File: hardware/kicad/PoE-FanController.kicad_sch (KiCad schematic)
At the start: 26 parts, among them J2 FAN1, J3 FAN2, J4 FAN3, J5 FAN4, J8 Waveshare_ESP32P4POEETH, U1 LM2587-12

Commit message: hw+fw: add orange prog/OTA LED (issue #89)
Hardware:
- R13 (330Ω THT, P7.62mm) placed at PCB (25, 64)
- LED2 (orange 3mm THT, Wurth 150060AS75000) placed at PCB (31, 58)
  next to LED1 (green status LED)
- Circuit: PROG_LED → R13 → PROG_LED_A → LED2 anode → GND
- J8 pin 22 (GPIO15) wired to PROG_LED net (was NC)
- ERC: 0 errors · DRC: 0 real errors · 0 courtyard overlaps
- BOM updated with R13 and LED2 entries

Firmware:
- pins.h: add PROG_LED_PIN (GPIO15)
- ota.cpp: add ota_init() to configure GPIO15; LED2 flickers on each
  OTA chunk write, holds HIGH on success, LOW on error
- main.cpp: call ota_init() in setup()

Co-authored-by: Copilot <223556219+Copilot@users.noreply.github.com>
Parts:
- added LED2: LED_ORANGE, LED_THT:LED_D3.0mm, symbol Custom:LED
- added R4: 10k, Resistor_THT:R_Axial_DIN0207_L6.3mm_D2.5mm_P7.62mm_Horizontal, symbol Custom:R
- R13: renamed from R4; value 10k -> 330R
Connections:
- net NTC_ADC: now also R4.2; no longer R13.2
- net PROG_LED: now reaches R13.1
- net PROG_LED: now also J8.22 (NC)
- new net PROG_LED_A: LED2.1 (A), R13.2
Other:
- note added: "Prog LED (OTA)"
- moved on the sheet: R13

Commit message: hw(oq): resolve OQ-02 — fix +5V pins on J8 (39/40 not 2/4)
Confirmed from Waveshare ESP32-P4-ETH schematic (Interface section):
  - Pin 39 = VSYS: +5V PoE PD main output
  - Pin 40 = VBUS: +5V USB source
  - Pins 2 and 4 are NOT power pins (previously wrong assumption)

Changes in components.py:
  - J8 pin 39: NC -> +5V power_out (VSYS)
  - J8 pin 40: NC -> +5V power_out (VBUS)
  - J8 pin 2:  +5V power_out -> NC
  - J8 pin 4:  +5V power_out -> NC
  - Clear OQ-02 PENDING marker
  - Update placement net connections accordingly

Schematic regenerated; ERC: 0 errors; DRC: 0 errors.

Closes #85

Co-authored-by: Copilot <223556219+Copilot@users.noreply.github.com>
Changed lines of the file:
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@@
     (instances (project "PoE-FanController" (path "/" (reference "#PWR039") (unit 1))))
   )
-  (symbol (lib_id "power:+5V") (at 106.6800 128.2700 0)
+  (symbol (lib_id "power:+5V") (at 76.2000 176.5300 0)
     (unit 1) (exclude_from_sim no) (in_bom yes) (on_board yes) (dnp no)
     (fields_autoplaced yes)
     (property "Reference" "#PWR040"
-      (at 106.6800 130.8100 0)
+      (at 76.2000 179.0700 0)
       (hide yes)
       (effects (font (size 1.27 1.27))))
     (property "Value" "+5V"
-      (at 106.6800 125.7300 0)
+      (at 76.2000 173.9900 0)
       (effects (font (size 1.27 1.27))))
     (property "Footprint" ""
-      (at 106.6800 128.2700 0)
+      (at 76.2000 176.5300 0)
       (hide yes)
       (effects (font (size 1.27 1.27))))
     (property "Datasheet" ""
-      (at 106.6800 128.2700 0)
+      (at 76.2000 176.5300 0)
       (hide yes)
       (effects (font (size 1.27 1.27))))
@@
     (instances (project "PoE-FanController" (path "/" (reference "#PWR040") (unit 1))))
   )
-  (symbol (lib_id "power:+5V") (at 106.6800 130.8100 0)
+  (symbol (lib_id "power:GND") (at 106.6800 133.3500 0)
     (unit 1) (exclude_from_sim no) (in_bom yes) (on_board yes) (dnp no)
     (fields_autoplaced yes)
     (property "Reference" "#PWR041"
-      (at 106.6800 133.3500 0)
-      (hide yes)
-      (effects (font (size 1.27 1.27))))
-    (property "Value" "+5V"
-      (at 106.6800 128.2700 0)
-      (effects (font (size 1.27 1.27))))
-    (property "Footprint" ""
-      (at 106.6800 130.8100 0)
-      (hide yes)
-      (effects (font (size 1.27 1.27))))
-    (property "Datasheet" ""
-      (at 106.6800 130.8100 0)
-      (hide yes)
-      (effects (font (size 1.27 1.27))))
-    (pin "1")
-    (instances (project "PoE-FanController" (path "/" (reference "#PWR041") (unit 1))))
-  )
-  (symbol (lib_id "power:GND") (at 106.6800 133.3500 0)
-    (unit 1) (exclude_from_sim no) (in_bom yes) (on_board yes) (dnp no)
-    (fields_autoplaced yes)
-    (property "Reference" "#PWR042"
       (at 106.6800 135.8900 0)
       (hide yes)
@@
       (effects (font (size 1.27 1.27))))
     (pin "1")
-    (instances (project "PoE-FanController" (path "/" (reference "#PWR042") (unit 1))))
+    (instances (project "PoE-FanController" (path "/" (reference "#PWR041") (unit 1))))
   )
   (global_label "FAN2_PWM"
@@
     (unit 1) (exclude_from_sim no) (in_bom yes) (on_board yes) (dnp no)
     (fields_autoplaced yes)
-    (property "Reference" "#PWR043"
+    (property "Reference" "#PWR042"
       (at 106.6800 146.0500 0)
       (hide yes)
@@
       (effects (font (size 1.27 1.27))))
     (pin "1")
-    (instances (project "PoE-FanController" (path "/" (reference "#PWR043") (unit 1))))
+    (instances (project "PoE-FanController" (path "/" (reference "#PWR042") (unit 1))))
   )
   (global_label "FAN4_TACH"
@@
     (unit 1) (exclude_from_sim no) (in_bom yes) (on_board yes) (dnp no)
     (fields_autoplaced yes)
-    (property "Reference" "#PWR044"
+    (property "Reference" "#PWR043"
       (at 106.6800 153.6700 0)
       (hide yes)
@@
       (effects (font (size 1.27 1.27))))
     (pin "1")
-    (instances (project "PoE-FanController" (path "/" (reference "#PWR044") (unit 1))))
+    (instances (project "PoE-FanController" (path "/" (reference "#PWR043") (unit 1))))
   )
   (global_label "PROG_LED"
@@
     (unit 1) (exclude_from_sim no) (in_bom yes) (on_board yes) (dnp no)
     (fields_autoplaced yes)
-    (property "Reference" "#PWR045"
+    (property "Reference" "#PWR044"
       (at 106.6800 176.5300 0)
       (hide yes)
@@
       (hide yes)
       (effects (font (size 1.27 1.27))))
+    (pin "1")
+    (instances (project "PoE-FanController" (path "/" (reference "#PWR044") (unit 1))))
+  )
+  (symbol (lib_id "power:+5V") (at 106.6800 176.5300 0)
+    (unit 1) (exclude_from_sim no) (in_bom yes) (on_board yes) (dnp no)
+    (fields_autoplaced yes)
+    (property "Reference" "#PWR045"
+      (at 106.6800 179.0700 0)
+      (hide yes)
+      (effects (font (size 1.27 1.27))))
+    (property "Value" "+5V"
+      (at 106.6800 173.9900 0)
+      (effects (font (size 1.27 1.27))))
+    (property "Footprint" ""
+      (at 106.6800 176.5300 0)
+      (hide yes)
+      (effects (font (size 1.27 1.27))))
+    (property "Datasheet" ""
+      (at 106.6800 176.5300 0)
+      (hide yes)
+      (effects (font (size 1.27 1.27))))

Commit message: hw(schematic): add J6/R14/R15/LED6 and DS18B20_DATA/PROBE_LED nets
T001: Add Conn_1x03 (J6 Molex KK-254), R14 (4.7kΩ pull-up), R15 (330Ω),
      LED6 (green 3mm) to schematic generator with section header.
T002: Update J8 symbol/placement — pin 27 NC→DS18B20_DATA (GPIO19),
      pin 28 NC→PROBE_LED (GPIO20).
T003: Regenerated PoE-FanController.kicad_sch — J6/R14/R15/LED6 confirmed present.
T004: ERC clean — 0 errors, 83 pre-existing warnings (lib_symbol_mismatch).

Closes #101
Closes #102
Closes #103
Closes #104
Issue: #97

Co-authored-by: Copilot <223556219+Copilot@users.noreply.github.com>
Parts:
- added J6: Molex_KK254_3pin, Connector_Molex:Molex_KK-254_AE-6410-03A_1x03_P2.54mm_Vertical, symbol Custom:Conn_1x03
- added LED6: LED_GREEN, LED_THT:LED_D3.0mm, symbol Custom:LED
- added R14: 4k7, Resistor_THT:R_Axial_DIN0207_L6.3mm_D2.5mm_P7.62mm_Horizontal, symbol Custom:R
- added R15: 330R, Resistor_THT:R_Axial_DIN0207_L6.3mm_D2.5mm_P7.62mm_Horizontal, symbol Custom:R
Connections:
- net DS18B20_DATA: now reaches J8.27 (DS18B20_DATA)
- net DS18B20_DATA: now also J6.2 (DATA), R14.2
- net PROBE_LED: now reaches J8.28 (PROBE_LED)
- net PROBE_LED: now also R15.1
- new net PROBE_LED_A: LED6.1 (A), R15.2
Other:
- note added: "DS18B20 Temperature Probe (J6 / R14 / R15 / LED6)"

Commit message: hw: replace J2-J5 fan headers with keyed Molex KK-254 footprints (#100)
* docs(#100): add feature spec and technical plan for keyed fan headers

Add planning artifacts for Issue #100 - replacing unkeyed J2-J5 pin header
footprints with shrouded Molex KK-254 keyed connectors.

Key decisions documented in plan.md:
- Target footprint: Connector_Molex:Molex_KK-254_AE-6410-04A_1x04_P2.54mm_Vertical
  (22-23-2041 named in issue not present in KiCad 10.0 library; AE-6410-04A is
  the standard-library equivalent — same family, confirmed available)
- J6 already uses the 3-pin sibling (AE-6410-03A); this is established precedent
- Two generator edits required: s.define() + s.component() in components.py
- PCB: manual KiCad GUI only per P-KI-07; courtyard grows from ~2mm to 6.8mm
  perpendicular to pin row — documented with clearance assessment
- BOM §2.2 MAJOR amendment required (47053-1000 → 22-23-2041)
- No firmware changes, no isolation concerns, no power budget impact

Satisfies constitution principle P-HW-09 (amendment v3.2.0).

Files added:
  docs/features/keyed-fan-headers/spec.md
  docs/features/keyed-fan-headers/plan.md

* fix(docs): update constitution version and amend J2–J5 BOM to keyed headers

* docs: add architecture notes for keyed fan headers (J2–J5) feature

* docs(#100): add task breakdown and GitHub sub-issues for keyed fan headers (T001-T009, issues #120-#128)

* hw(#100): update J2-J5 footprint in generator and regenerate schematic

- T001: add Connector_Molex library entry to hardware/kicad/fp-lib-table
- T002: update Fan_Header define() and component() footprint to
  Connector_Molex:Molex_KK-254_AE-6410-04A_1x04_P2.54mm_Vertical
- T002: update Fan_Header datasheet URL to Molex 22-23-2041 product page
- T003: regenerate PoE-FanController.kicad_sch (4 instances updated)
- T004: ERC passes - 0 error-severity violations

Refs #120
Refs #121
Refs #122
Refs #123

Co-authored-by: Copilot <223556219+Copilot@users.noreply.github.com>

* hw(#100): swap J2-J5 PCB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
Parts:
- J2, J3, J4, J5: footprint Connector_PinHeader_2.54mm:PinHeader_1x04_P2.54mm_Vertical -> Connector_Molex:Molex_KK-254_AE-6410-04A_1x04_P2.54mm_Vertical
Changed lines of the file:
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@@
       (at 331.4700 82.5500 0)
       (effects (font (size 1.27 1.27))))
-    (property "Footprint" "Connector_PinHeader_2.54mm:PinHeader_1x04_P2.54mm_Vertical"
+    (property "Footprint" "Connector_Molex:Molex_KK-254_AE-6410-04A_1x04_P2.54mm_Vertical"
       (at 330.2000 81.2800 0)
       (hide yes)
@@
       (at 331.4700 113.0300 0)
       (effects (font (size 1.27 1.27))))
-    (property "Footprint" "Connector_PinHeader_2.54mm:PinHeader_1x04_P2.54mm_Vertical"
+    (property "Footprint" "Connector_Molex:Molex_KK-254_AE-6410-04A_1x04_P2.54mm_Vertical"
       (at 330.2000 111.7600 0)
       (hide yes)
@@
       (at 331.4700 143.5100 0)
       (effects (font (size 1.27 1.27))))
-    (property "Footprint" "Connector_PinHeader_2.54mm:PinHeader_1x04_P2.54mm_Vertical"
+    (property "Footprint" "Connector_Molex:Molex_KK-254_AE-6410-04A_1x04_P2.54mm_Vertical"
       (at 330.2000 142.2400 0)
       (hide yes)
@@
       (at 331.4700 173.9900 0)
       (effects (font (size 1.27 1.27))))
-    (property "Footprint" "Connector_PinHeader_2.54mm:PinHeader_1x04_P2.54mm_Vertical"
+    (property "Footprint" "Connector_Molex:Molex_KK-254_AE-6410-04A_1x04_P2.54mm_Vertical"
       (at 330.2000 172.7200 0)
       (hide yes)

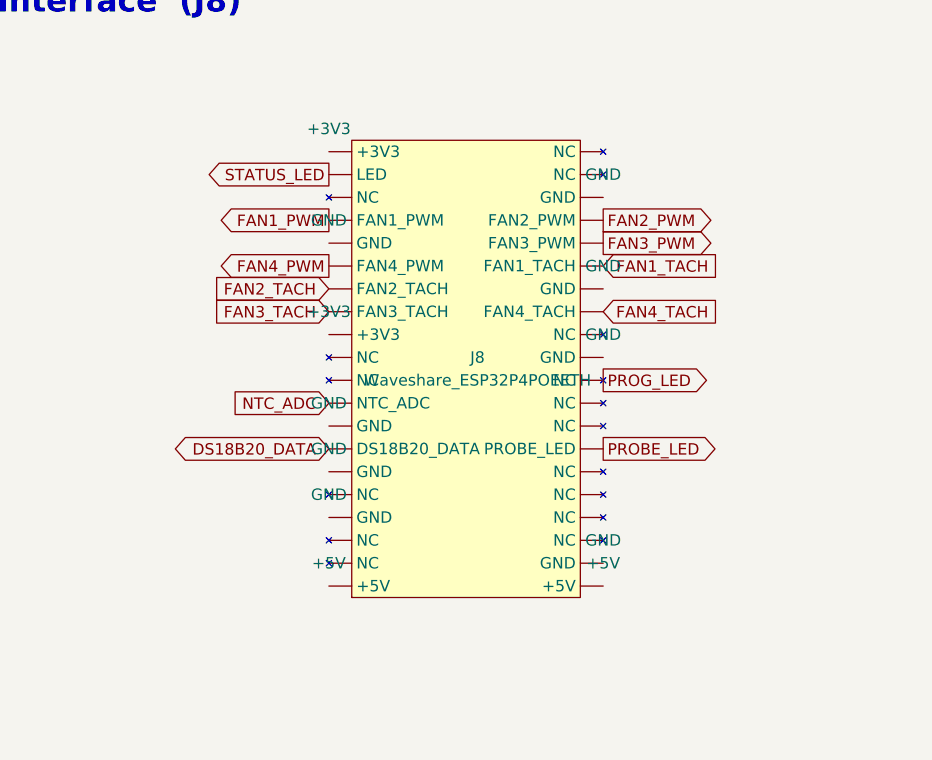
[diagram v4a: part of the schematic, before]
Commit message: fix(hw): correct J8 pin layout to consecutive columns (#133)
The Waveshare ESP32-P4-POE-ETH (SKU 32088) 2x20 header uses CONSECUTIVE
column numbering, not PICO-style alternating odd/even:
  Row A (y=-7.69mm): pads  1..20  (top → bottom)
  Row B (y=+7.69mm): pads 21..40  (top → bottom)

Changes:
- generator/components.py: rewrite Custom:J8_Waveshare symbol definition
  with pins 1-20 on left and pins 21-40 on right; update wiring section
  to match new side assignments (FAN2_PWM/FAN3_PWM/FAN1_TACH/FAN4_TACH
  move to left; NTC_ADC/DS18B20_DATA/+5V(VSYS) move to right)
- generator/gen_footprint_j8.py: change pad numbering from odd/even
  interleaving to consecutive rows (row_a=i+1, row_b=i+21)
- Regenerated PoE-FanController.kicad_sch via generate_project.py
- Regenerated PinSocket_2x20_P2.54mm_P15.38mm_Vertical.kicad_mod
- ERC: 0 errors, 81 pre-existing lib_symbol_mismatch warnings

Critical fix: pin 39 (+5V VSYS) now correctly on Row B (right side),
ensuring the boost converter input is wired to the actual PoE 5V rail.

Co-authored-by: Copilot <223556219+Copilot@users.noreply.github.com>
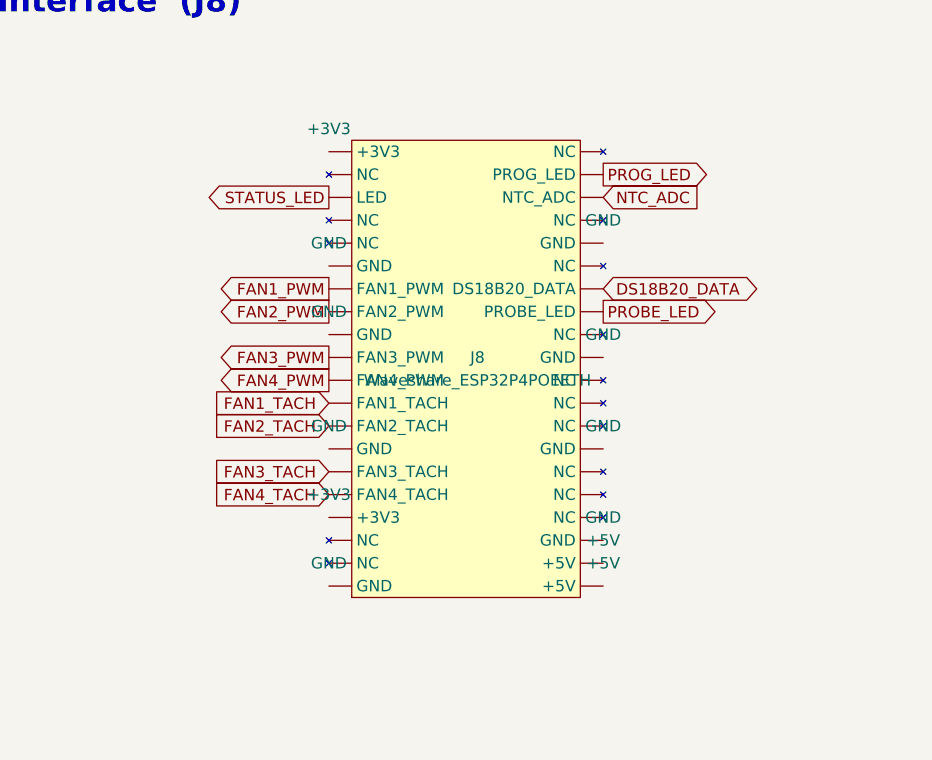
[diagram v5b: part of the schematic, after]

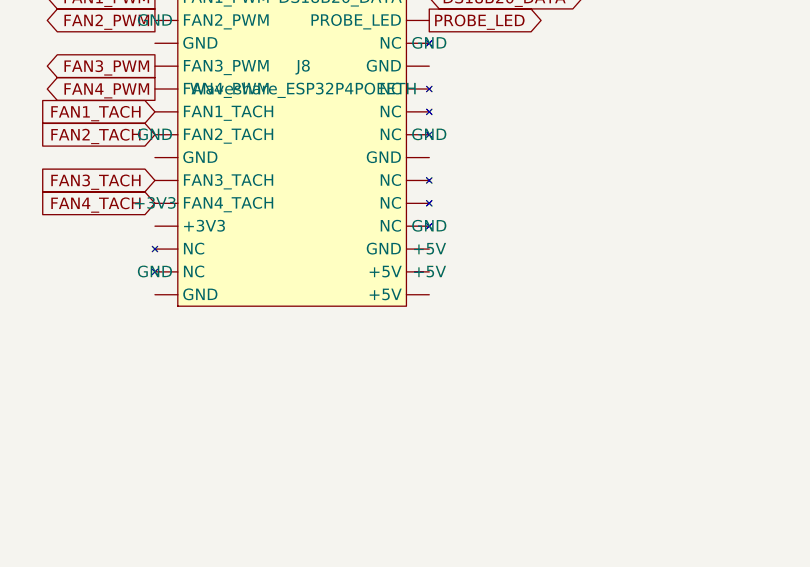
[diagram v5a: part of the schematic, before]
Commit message: fix(hw): leave J8 pin 40 (VBUS) as NC to prevent back-feed
When powered by PoE only (primary use case), pin 40 VBUS = 0V.
Connecting it to the +5V net would back-drive the Waveshare board's
USB VBUS rail through the daughter board trace.

Pin 39 (VSYS, PoE PD output) is the sole +5V source for U_BOOST.
Pin 40 (VBUS) is now NC, matching its no_connect symbol pin type.

ERC: 0 errors (80 pre-existing lib warnings)
DRC: 0 errors, 17 warnings, 71 unconnected (baseline restored)

Co-authored-by: Copilot <223556219+Copilot@users.noreply.github.com>
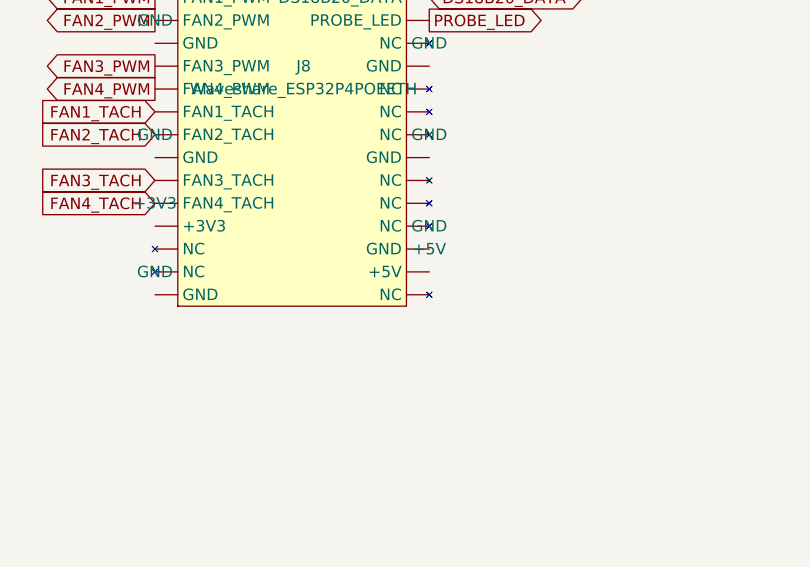
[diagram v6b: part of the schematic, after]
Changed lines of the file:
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@@
     (instances (project "PoE-FanController" (path "/" (reference "#PWR048") (unit 1))))
-  )
-  (symbol (lib_id "power:+5V") (at 106.6800 176.5300 0)
-    (unit 1) (exclude_from_sim no) (in_bom yes) (on_board yes) (dnp no)
-    (fields_autoplaced yes)
-    (property "Reference" "#PWR049"
-      (at 106.6800 179.0700 0)
-      (hide yes)
-      (effects (font (size 1.27 1.27))))
-    (property "Value" "+5V"
-      (at 106.6800 173.9900 0)
-      (effects (font (size 1.27 1.27))))
-    (property "Footprint" ""
-      (at 106.6800 176.5300 0)
-      (hide yes)
-      (effects (font (size 1.27 1.27))))
-    (property "Datasheet" ""
-      (at 106.6800 176.5300 0)
-      (hide yes)
-      (effects (font (size 1.27 1.27))))
-    (pin "1")
-    (instances (project "PoE-FanController" (path "/" (reference "#PWR049") (unit 1))))
   )
   (sheet_instances (path "/" (page "1")))
